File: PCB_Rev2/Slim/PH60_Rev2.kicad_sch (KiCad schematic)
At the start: 30 parts, among them J1 USB_C_Receptacle_USB2.0_16P, J2 Conn_01x02, U2 W25Q128JVS, U3 RP2040, U4 XC6206PxxxMR, Y1 Crystal_GND24

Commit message: Add mounting hole.
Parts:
- added F1: 500ma, Fuse:Fuse_0402_1005Metric, symbol Device:Polyfuse_Small
- added H1, H2, H3, H4, H5, H6: MountingHole, MountingHole:MountingHole_2.2mm_M2, symbol Mechanical:MountingHole
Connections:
- net VBUS: now also F1.2; no longer J1.A4 (VBUS), J1.A9 (VBUS), J1.B4 (VBUS), J1.B9 (VBUS)
- net RGB_IN: now reaches U3.34 (GPIO22)
- net DIN: no longer names the net of U3.32 (GPIO21)
- new net: F1.1, J1.A4 (VBUS), J1.A9 (VBUS), J1.B4 (VBUS), J1.B9 (VBUS)

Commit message: Change fuse to 0603 for better performance
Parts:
- F1: footprint Fuse:Fuse_0402_1005Metric -> Fuse:Fuse_0603_1608Metric
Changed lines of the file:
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@@
 			)
 		)
-		(property "Footprint" "Fuse:Fuse_0402_1005Metric"
+		(property "Footprint" "Fuse:Fuse_0603_1608Metric"
 			(at 78.74 195.58 0)
 			(effects

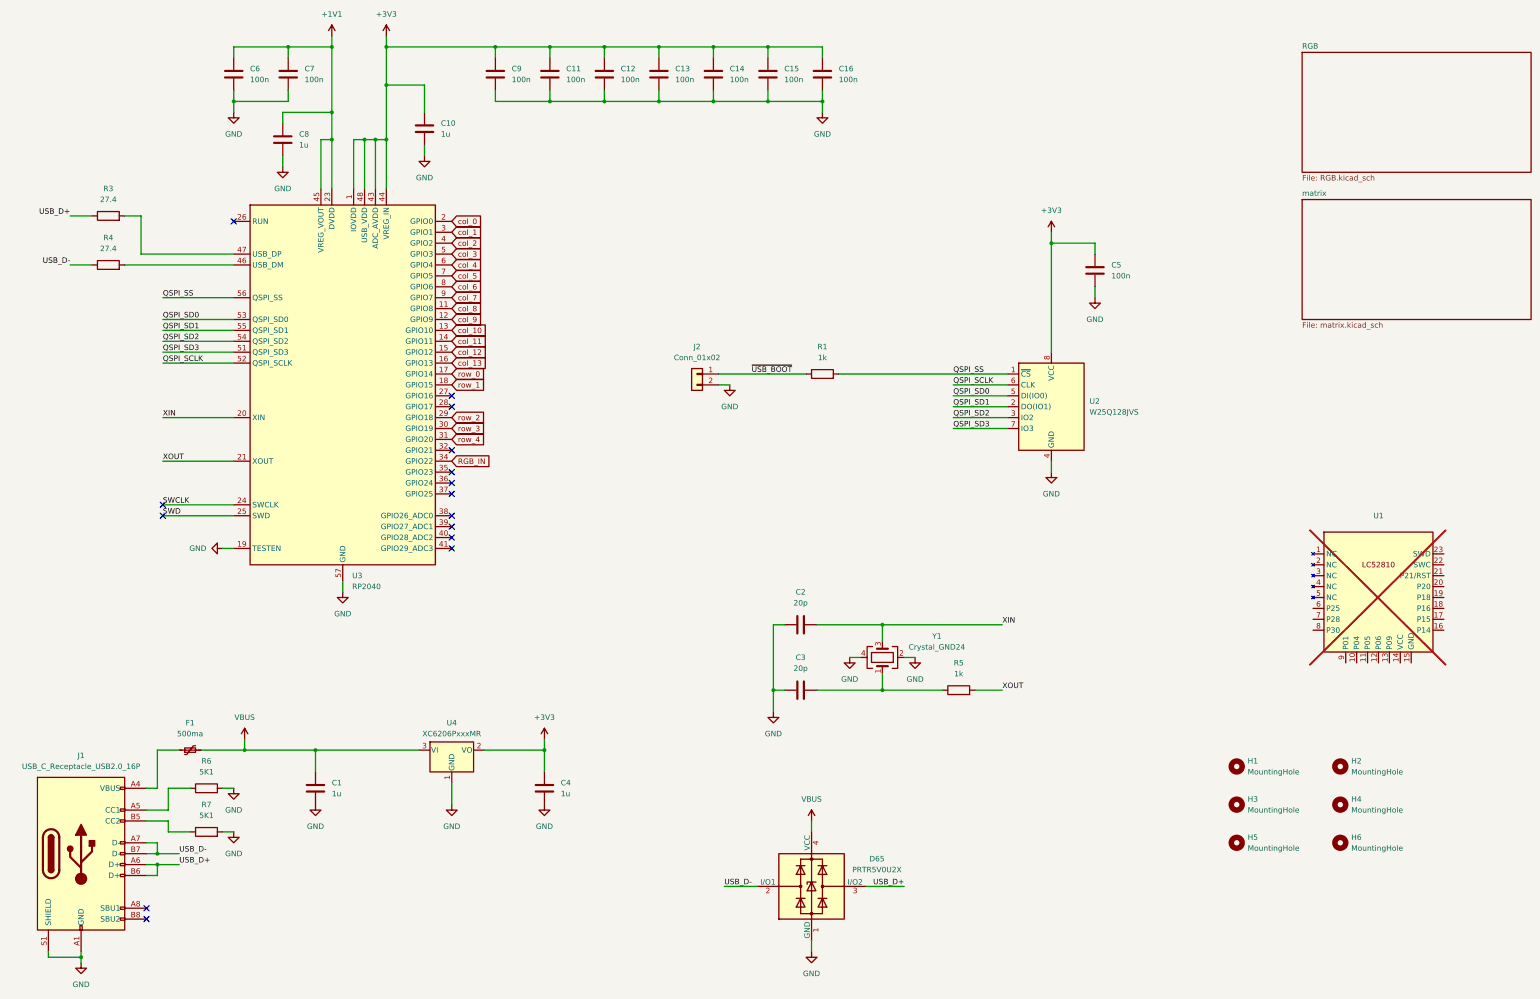
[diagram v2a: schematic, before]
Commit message: Recalculate USB resistor.
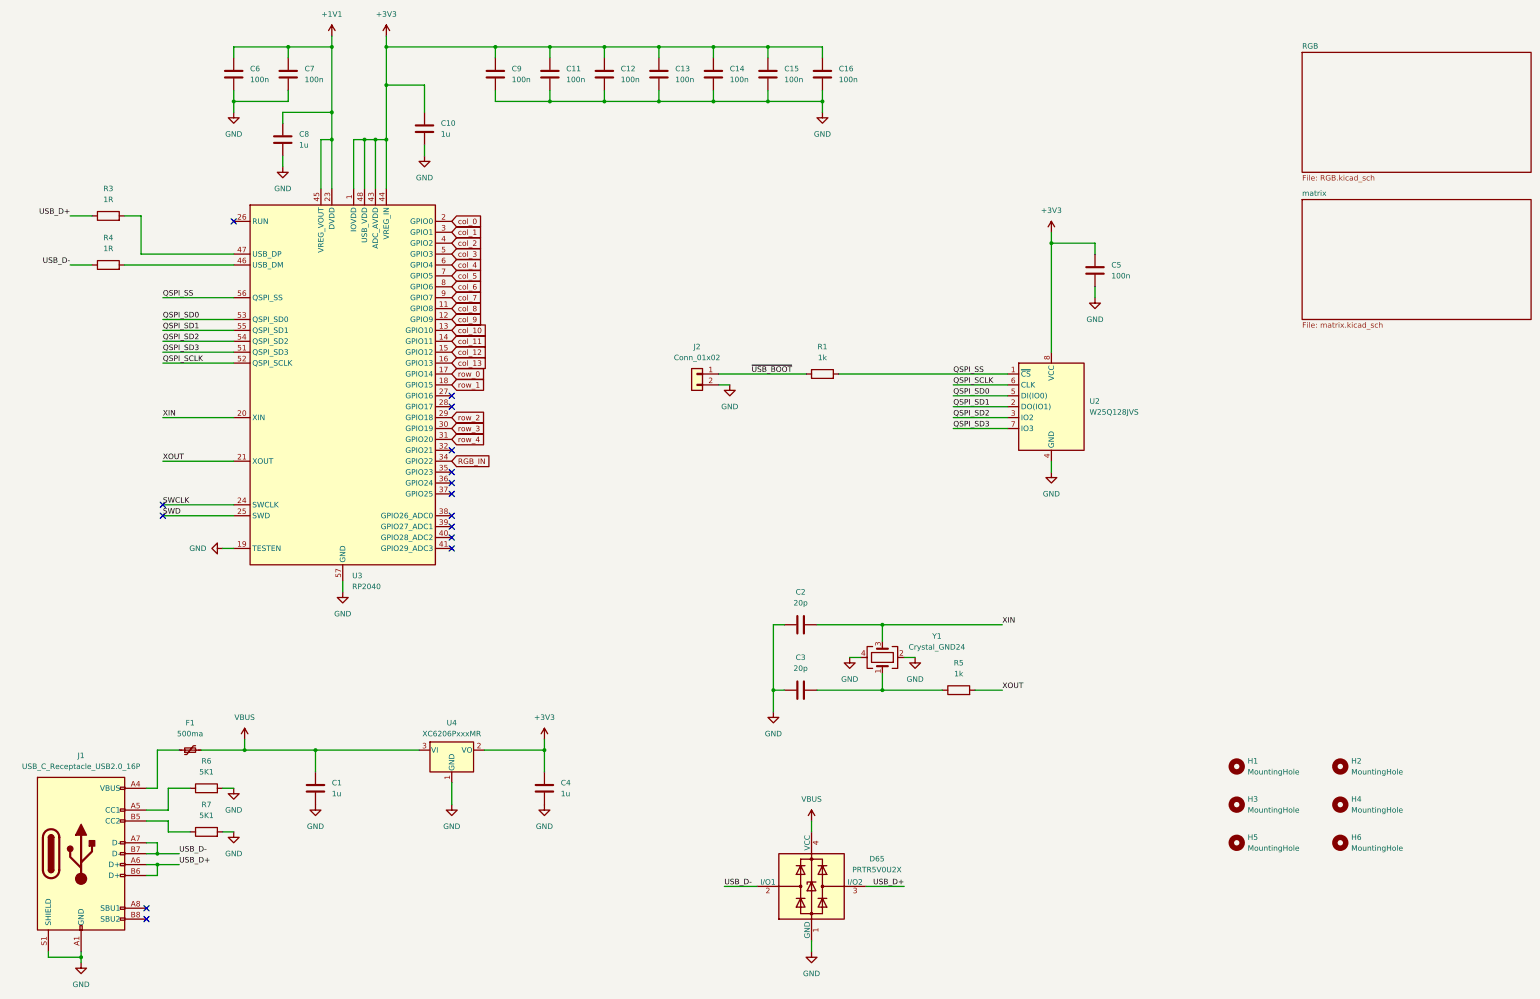
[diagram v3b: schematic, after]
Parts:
- removed U1: ~, nRF_Module:nRF52810_Module, symbol nRF52810_Module:LC52810
- R3, R4: value 27.4 -> 1R
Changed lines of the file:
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@@
 			)
 		)
-		(property "Value" "27.4"
+		(property "Value" "1R"
 			(at 54.61 80.01 90)
 			(effects
@@
 	)
 	(symbol
-		(lib_id "nRF52810_Module:LC52810")
-		(at 350.52 151.13 0)
-		(unit 1)
-		(exclude_from_sim no)
-		(in_bom yes)
-		(on_board no)
-		(dnp yes)
-		(fields_autoplaced yes)
-		(property "Reference" "U1"
-			(at 350.52 142.24 0)
-			(effects
-				(font
-					(size 1.27 1.27)
-				)
-			)
-		)
-		(property "Value" "~"
-			(at 350.52 144.78 0)
-			(effects
-				(font
-					(size 1.27 1.27)
-				)
-			)
-		)
-		(property "Footprint" "nRF_Module:nRF52810_Module"
-			(at 350.52 151.13 0)
-			(effects
-				(font
-					(size 1.27 1.27)
-				)
-				(hide yes)
-			)
-		)
-		(property "Datasheet" ""
-			(at 350.52 151.13 0)
-			(effects
-				(font
-					(size 1.27 1.27)
-				)
-				(hide yes)
-			)
-		)
-		(property "Description" ""
-			(at 350.52 151.13 0)
-			(effects
-				(font
-					(size 1.27 1.27)
-				)
-				(hide yes)
-			)
-		)
-		(pin "11"
-		)
-		(pin "14"
-		)
-		(pin "15"
-		)
-		(pin "8"
-		)
-		(pin "6"
-		)
-		(pin "21"
-		)
-		(pin "9"
-		)
-		(pin "17"
-		)
-		(pin "10"
-		)
-		(pin "3"
-		)
-		(pin "22"
-		)
-		(pin "23"
-		)
-		(pin "1"
-		)
-		(pin "18"
-		)
-		(pin "5"
-		)
-		(pin "16"
-		)
-		(pin "2"
-		)
-		(pin "20"
-		)
-		(pin "7"
-		)
-		(pin "12"
-		)
-		(pin "19"
-		)
-		(pin "4"
-		)
-		(pin "13"
-		)
-		(instances
-			(project ""
-				(path "/dca0f898-8fdb-4522-a51d-f4f4238906e7"
-					(reference "U1")
-					(unit 1)
-				)
-			)
-		)
-	)
-	(symbol
 		(lib_id "Device:C")
 		(at 156.21 205.74 0)
@@
 			)
 		)
-		(property "Value" "27.4"
+		(property "Value" "1R"
 			(at 54.61 68.58 90)
 			(effects
